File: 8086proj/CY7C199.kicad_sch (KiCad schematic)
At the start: 5 parts, among them U3 CY7C199, U4 CY7C199

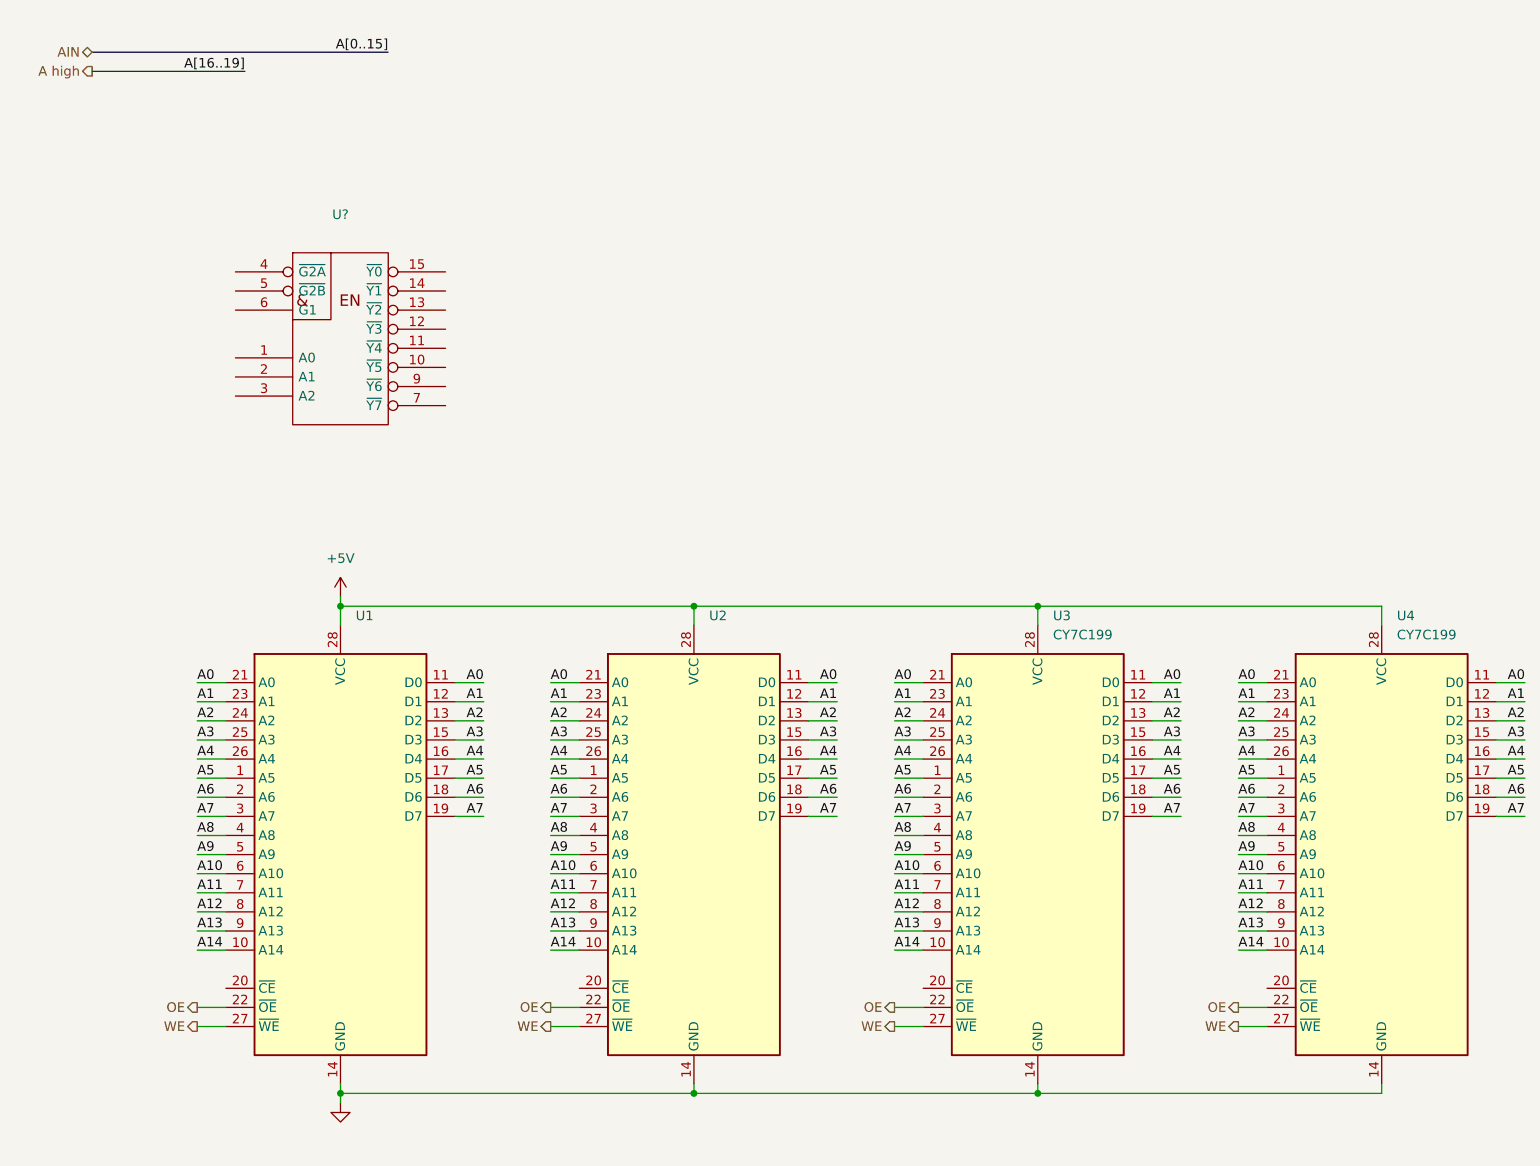
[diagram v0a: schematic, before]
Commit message: finished cy7c199
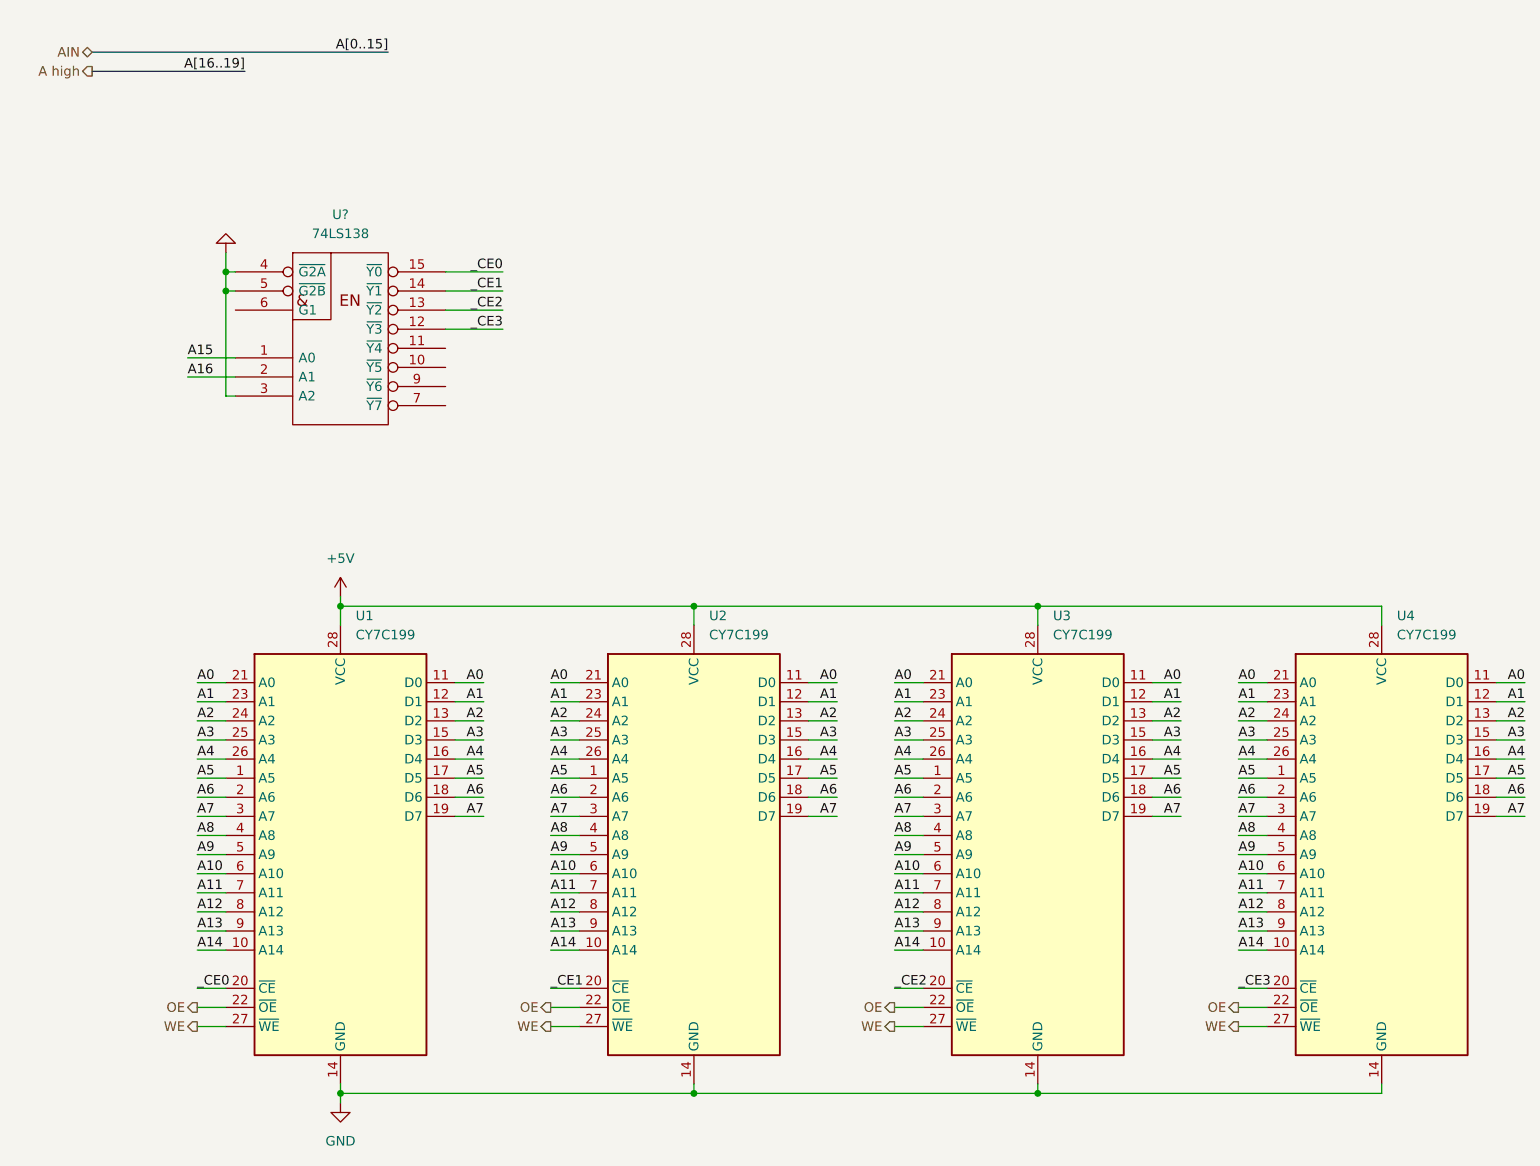
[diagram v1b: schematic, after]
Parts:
- U1, U2: value (none) -> CY7C199
- U?: value (none) -> 74LS138
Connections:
- net GND: now also U?.3 (A2), U?.4 (~{G2A}), U?.5 (~{G2B})
- net _CE3: now reaches U4.20 (~{CE})
- net _CE3: now also U?.12 (~{Y3})
- net _CE1: now reaches U2.20 (~{CE})
- net _CE1: now also U?.14 (~{Y1})
- net _CE0: now reaches U1.20 (~{CE})
- net _CE0: now also U?.15 (~{Y0})
- net A15: now reaches U?.1 (A0)
- net _CE2: now reaches U?.13 (~{Y2})
- net _CE2: now also U3.20 (~{CE})
- net A16: now reaches U?.2 (A1)
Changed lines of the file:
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@@
 (kicad_sch (version 20211123) (generator eeschema)
   (paper "A4")
+  (junction (at 52.07 49.53) (diameter 0) (color 0 0 0 0)
+  )
   (junction (at 67.31 156.21) (diameter 0) (color 0 0 0 0)
   )
   (junction (at 114.3 156.21) (diameter 0) (color 0 0 0 0)
   )
+  (junction (at 52.07 46.99) (diameter 0) (color 0 0 0 0)
+  )
   (junction (at 160.02 156.21) (diameter 0) (color 0 0 0 0)
   )
@@
     (stroke (width 0) (type default) (color 0 0 0 0))
   )
+  (wire (pts (xy 186.69 142.24) (xy 190.5 142.24))
+    (stroke (width 0) (type default) (color 0 0 0 0))
+  )
   (wire (pts (xy 220.98 109.22) (xy 224.79 109.22))
     (stroke (width 0) (type default) (color 0 0 0 0))
@@
     (stroke (width 0) (type default) (color 0 0 0 0))
   )
+  (wire (pts (xy 52.07 49.53) (xy 53.34 49.53))
+    (stroke (width 0) (type default) (color 0 0 0 0))
+  )
   (wire (pts (xy 140.97 104.14) (xy 144.78 104.14))
     (stroke (width 0) (type default) (color 0 0 0 0))
   )
+  (wire (pts (xy 46.99 60.96) (xy 53.34 60.96))
+    (stroke (width 0) (type default) (color 0 0 0 0))
+  )
   (wire (pts (xy 186.69 134.62) (xy 190.5 134.62))
     (stroke (width 0) (type default) (color 0 0 0 0))
@@
     (stroke (width 0) (type default) (color 0 0 0 0))
   )
+  (wire (pts (xy 52.07 46.99) (xy 53.34 46.99))
+    (stroke (width 0) (type default) (color 0 0 0 0))
+  )
   (wire (pts (xy 67.31 154.94) (xy 67.31 156.21))
     (stroke (width 0) (type default) (color 0 0 0 0))
@@
     (stroke (width 0) (type default) (color 0 0 0 0))
   )
+  (wire (pts (xy 95.25 142.24) (xy 99.06 142.24))
+    (stroke (width 0) (type default) (color 0 0 0 0))
+  )
   (wire (pts (xy 129.54 104.14) (xy 133.35 104.14))
     (stroke (width 0) (type default) (color 0 0 0 0))
@@
     (stroke (width 0) (type default) (color 0 0 0 0))
   )
+  (wire (pts (xy 52.07 44.45) (xy 52.07 46.99))
+    (stroke (width 0) (type default) (color 0 0 0 0))
+  )
   (wire (pts (xy 95.25 109.22) (xy 99.06 109.22))
     (stroke (width 0) (type default) (color 0 0 0 0))
@@
     (stroke (width 0) (type default) (color 0 0 0 0))
   )
+  (wire (pts (xy 46.99 58.42) (xy 53.34 58.42))
+    (stroke (width 0) (type default) (color 0 0 0 0))
+  )
   (wire (pts (xy 140.97 127) (xy 144.78 127))
     (stroke (width 0) (type default) (color 0 0 0 0))
@@
     (stroke (width 0) (type default) (color 0 0 0 0))
   )
+  (wire (pts (xy 81.28 46.99) (xy 88.9 46.99))
+    (stroke (width 0) (type default) (color 0 0 0 0))
+  )
   (wire (pts (xy 82.55 104.14) (xy 86.36 104.14))
     (stroke (width 0) (type default) (color 0 0 0 0))
@@
     (stroke (width 0) (type default) (color 0 0 0 0))
   )
+  (wire (pts (xy 48.26 142.24) (xy 52.07 142.24))
+    (stroke (width 0) (type default) (color 0 0 0 0))
+  )
   (wire (pts (xy 186.69 147.32) (xy 190.5 147.32))
     (stroke (width 0) (type default) (color 0 0 0 0))
@@
     (stroke (width 0) (type default) (color 0 0 0 0))
   )
+  (wire (pts (xy 52.07 46.99) (xy 52.07 49.53))
+    (stroke (width 0) (type default) (color 0 0 0 0))
+  )
   (wire (pts (xy 48.26 101.6) (xy 52.07 101.6))
     (stroke (width 0) (type default) (color 0 0 0 0))
   )
+  (wire (pts (xy 81.28 52.07) (xy 88.9 52.07))
+    (stroke (width 0) (type default) (color 0 0 0 0))
+  )
   (wire (pts (xy 114.3 91.44) (xy 114.3 93.98))
     (stroke (width 0) (type default) (color 0 0 0 0))
@@
     (stroke (width 0) (type default) (color 0 0 0 0))
   )
+  (wire (pts (xy 53.34 63.5) (xy 52.07 63.5))
+    (stroke (width 0) (type default) (color 0 0 0 0))
+  )
+  (wire (pts (xy 81.28 54.61) (xy 88.9 54.61))
+    (stroke (width 0) (type default) (color 0 0 0 0))
+  )
   (wire (pts (xy 95.25 101.6) (xy 99.06 101.6))
     (stroke (width 0) (type default) (color 0 0 0 0))
@@
     (stroke (width 0) (type default) (color 0 0 0 0))
   )
+  (wire (pts (xy 52.07 49.53) (xy 52.07 63.5))
+    (stroke (width 0) (type default) (color 0 0 0 0))
+  )
   (wire (pts (xy 48.26 104.14) (xy 52.07 104.14))
     (stroke (width 0) (type default) (color 0 0 0 0))
@@
     (stroke (width 0) (type default) (color 0 0 0 0))
   )
+  (wire (pts (xy 81.28 49.53) (xy 88.9 49.53))
+    (stroke (width 0) (type default) (color 0 0 0 0))
+  )
   (wire (pts (xy 48.26 127) (xy 52.07 127))
     (stroke (width 0) (type default) (color 0 0 0 0))
@@
     (stroke (width 0) (type default) (color 0 0 0 0))
   )
+  (wire (pts (xy 140.97 142.24) (xy 144.78 142.24))
+    (stroke (width 0) (type default) (color 0 0 0 0))
+  )
   (wire (pts (xy 186.69 104.14) (xy 190.5 104.14))
     (stroke (width 0) (type default) (color 0 0 0 0))
@@
     (effects (font (size 1.27 1.27)) (justify left bottom))
   )
+  (label "_CE3" (at 186.69 142.24 0)
+    (effects (font (size 1.27 1.27)) (justify left bottom))
+  )
   (label "A0" (at 86.36 101.6 180)
     (effects (font (size 1.27 1.27)) (justify right bottom))
@@
     (effects (font (size 1.27 1.27)) (justify left bottom))
   )
+  (label "_CE2" (at 140.97 142.24 0)
+    (effects (font (size 1.27 1.27)) (justify left bottom))
+  )
   (label "A7" (at 48.26 119.38 0)
     (effects (font (size 1.27 1.27)) (justify left bottom))
@@
     (effects (font (size 1.27 1.27)) (justify left bottom))
   )
+  (label "_CE0" (at 88.9 46.99 180)
+    (effects (font (size 1.27 1.27)) (justify right bottom))
+  )
   (label "A8" (at 140.97 121.92 0)
     (effects (font (size 1.27 1.27)) (justify left bottom))
@@
     (effects (font (size 1.27 1.27)) (justify left bottom))
   )
+  (label "A15" (at 46.99 58.42 0)
+    (effects (font (size 1.27 1.27)) (justify left bottom))
+  )
   (label "A11" (at 95.25 129.54 0)
     (effects (font (size 1.27 1.27)) (justify left bottom))
   )
+  (label "_CE3" (at 88.9 54.61 180)
+    (effects (font (size 1.27 1.27)) (justify right bottom))
+  )
+  (label "_CE1" (at 88.9 49.53 180)
+    (effects (font (size 1.27 1.27)) (justify right bottom))
+  )
+  (label "_CE1" (at 95.25 142.24 0)
+    (effects (font (size 1.27 1.27)) (justify left bottom))
+  )
   (label "A2" (at 224.79 106.68 180)
     (effects (font (size 1.27 1.27)) (justify right bottom))
@@
     (effects (font (size 1.27 1.27)) (justify right bottom))
   )
+  (label "_CE2" (at 88.9 52.07 180)
+    (effects (font (size 1.27 1.27)) (justify right bottom))
+  )
   (label "A10" (at 140.97 127 0)
     (effects (font (size 1.27 1.27)) (justify left bottom))
@@
     (effects (font (size 1.27 1.27)) (justify right bottom))
   )
+  (label "A16" (at 46.99 60.96 0)
+    (effects (font (size 1.27 1.27)) (justify left bottom))
+  )
   (label "A6" (at 95.25 116.84 0)
     (effects (font (size 1.27 1.27)) (justify left bottom))
@@
   )
   (label "A8" (at 186.69 121.92 0)
+    (effects (font (size 1.27 1.27)) (justify left bottom))
+  )
+  (label "_CE0" (at 48.26 142.24 0)
     (effects (font (size 1.27 1.27)) (justify left bottom))
   )
@@
       (effects (font (size 1.27 1.27)) hide)
     )
-    (property "Value" "" (id 1) (at 67.31 162.56 0))
+    (property "Value" "GND" (id 1) (at 67.31 162.56 0))
     (property "Footprint" "" (id 2) (at 67.31 157.48 0)
       (effects (font (size 1.27 1.27)) hide)
@@
       (effects (font (size 1.27 1.27)) (justify left))
     )
-    (property "Value" "" (id 1) (at 116.3194 95.25 0)
+    (property "Value" "CY7C199" (id 1) (at 116.3194 95.25 0)
       (effects (font (size 1.27 1.27)) (justify left))
     )
@@
       (effects (font (size 1.27 1.27)) (justify left))
     )
-    (property "Value" "" (id 1) (at 69.3294 95.25 0)
+    (property "Value" "CY7C199" (id 1) (at 69.3294 95.25 0)
       (effects (font (size 1.27 1.27)) (justify left))
     )
@@
     (pin "9")
   )
+  (symbol (lib_id "power:GND") (at 52.07 44.45 180) (unit 1)
+    (in_bom yes) (on_board yes) (fields_autoplaced)
+    (property "Reference" "#PWR?" (id 0) (at 52.07 38.1 0)
+      (effects (font (size 1.27 1.27)) hide)
+    )
+    (property "Value" "" (id 1) (at 52.07 39.37 0))
+    (property "Footprint" "" (id 2) (at 52.07 44.45 0)
+      (effects (font (size 1.27 1.27)) hide)
+    )
+    (property "Datasheet" "" (id 3) (at 52.07 44.45 0)
+      (effects (font (size 1.27 1.27)) hide)
+    )
+    (pin "1")
+  )
   (symbol (lib_id "74xx_IEEE:74LS138") (at 67.31 52.07 0) (unit 1)
     (in_bom yes) (on_board yes) (fields_autoplaced)
     (property "Reference" "U?" (id 0) (at 67.31 39.37 0))
-    (property "Value" "" (id 1) (at 67.31 41.91 0))
+    (property "Value" "74LS138" (id 1) (at 67.31 41.91 0))
     (property "Footprint" "" (id 2) (at 67.31 52.07 0)
       (effects (font (size 1.27 1.27)) hide)

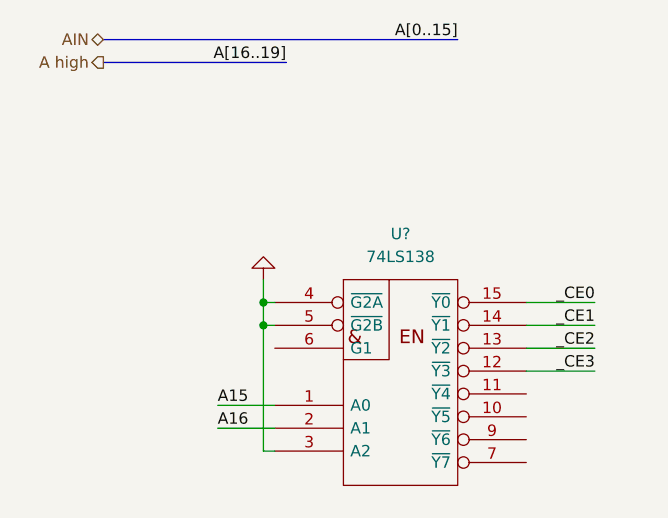
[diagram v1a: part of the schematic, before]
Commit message: 28F010 fix
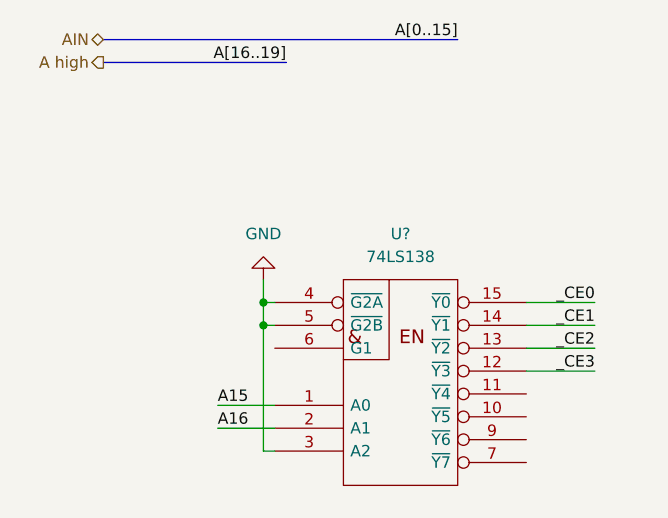
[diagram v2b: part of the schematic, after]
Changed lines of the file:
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@@
       (effects (font (size 1.27 1.27)) hide)
     )
-    (property "Value" "" (id 1) (at 52.07 39.37 0))
+    (property "Value" "GND" (id 1) (at 52.07 39.37 0))
     (property "Footprint" "" (id 2) (at 52.07 44.45 0)
       (effects (font (size 1.27 1.27)) hide)

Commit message: 8259
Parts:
- removed U?: 74LS138, symbol 74xx_IEEE:74LS138
- added C0, C1, C2, C3: (no value), symbol Device:C
- added C?: .1uF, symbol Device:C
- added U0: (no value), symbol Logic_Programmable:PAL16L8
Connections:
- net _CE2 is gone; now on net _CE1: U3.20 (~{CE})
- net _CE3 is gone; now on net _CE1: U4.20 (~{CE})
- net A0: no longer U1.11 (D0), U2.11 (D0), U3.11 (D0), U4.11 (D0)
- net A1: no longer U1.12 (D1), U2.12 (D1), U3.12 (D1), U4.12 (D1)
- net A16: now also U0.1 (I1)
- net A2: no longer U1.13 (D2), U2.13 (D2), U3.13 (D2), U4.13 (D2)
- net A3: no longer U1.15 (D3), U2.15 (D3), U3.15 (D3), U4.15 (D3)
- net A4: no longer U1.16 (D4), U2.16 (D4), U3.16 (D4), U4.16 (D4)
- net A5: no longer U1.17 (D5), U2.17 (D5), U3.17 (D5), U4.17 (D5)
- net A6: no longer U1.18 (D6), U2.18 (D6), U3.18 (D6), U4.18 (D6)
- net A7: no longer U1.19 (D7), U2.19 (D7), U3.19 (D7), U4.19 (D7)
- net GND: now also C0.1, C1.1, C2.1, C3.1, C?.1, U0.10 (GND)
- net _CE0: now also U2.20 (~{CE}), U0.19 (IO1)
- net _CE1: now also U0.18 (IO2); no longer U2.20 (~{CE})
- net +5V renamed VIN
- net VIN: now also C0.2, C1.2, C2.2, C3.2, C?.2, U0.20 (VCC)
- new net D0: U1.11 (D0), U3.11 (D0)
- new net D1: U1.12 (D1), U3.12 (D1)
- new net D10: U2.13 (D2), U4.13 (D2)
- new net D11: U2.15 (D3), U4.15 (D3)
- new net D12: U2.16 (D4), U4.16 (D4)
- new net D13: U2.17 (D5), U4.17 (D5)
- new net D14: U2.18 (D6), U4.18 (D6)
- new net D15: U2.19 (D7), U4.19 (D7)
- new net D2: U1.13 (D2), U3.13 (D2)
- new net D3: U1.15 (D3), U3.15 (D3)
- new net D4: U1.16 (D4), U3.16 (D4)
- new net D5: U1.17 (D5), U3.17 (D5)
- new net D6: U1.18 (D6), U3.18 (D6)
- new net D7: U1.19 (D7), U3.19 (D7)
- new net D8: U2.11 (D0), U4.11 (D0)
- new net D9: U2.12 (D1), U4.12 (D1)
- no-connect marks 0 -> 15

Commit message: fixes
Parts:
- C0, C1, C2, C3: value (none) -> .1uF
- U0: value (none) -> PAL16L8
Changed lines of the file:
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@@
       (effects (font (size 1.27 1.27)) (justify left))
     )
-    (property "Value" "" (id 1) (at 111.7599 83.82 0)
+    (property "Value" ".1uF" (id 1) (at 111.7599 83.82 0)
       (effects (font (size 1.27 1.27)) (justify left))
     )
@@
       (effects (font (size 1.27 1.27)) (justify left))
     )
-    (property "Value" "" (id 1) (at 203.1999 83.82 0)
+    (property "Value" ".1uF" (id 1) (at 203.1999 83.82 0)
       (effects (font (size 1.27 1.27)) (justify left))
     )
@@
       (effects (font (size 1.27 1.27)) hide)
     )
-    (property "Value" "" (id 1) (at 45.72 72.39 0))
+    (property "Value" "GND" (id 1) (at 45.72 72.39 0))
     (property "Footprint" "" (id 2) (at 45.72 67.31 0)
       (effects (font (size 1.27 1.27)) hide)
@@
       (effects (font (size 1.27 1.27)) (justify left))
     )
-    (property "Value" "" (id 1) (at 47.7394 35.56 0)
+    (property "Value" "PAL16L8" (id 1) (at 47.7394 35.56 0)
       (effects (font (size 1.27 1.27)) (justify left))
     )
@@
       (effects (font (size 1.27 1.27)) (justify left))
     )
-    (property "Value" "" (id 1) (at 64.7699 83.82 0)
+    (property "Value" ".1uF" (id 1) (at 64.7699 83.82 0)
       (effects (font (size 1.27 1.27)) (justify left))
     )
@@
       (effects (font (size 1.27 1.27)) (justify left))
     )
-    (property "Value" "" (id 1) (at 157.4799 83.82 0)
-      (effects (font (size 1.27 1.27)) (justify left))
-    )
+    (property "Value" ".1uF" (id 1) (at 157.4799 83.82 0)
+      (effects (font (size 1.27 1.27)) (justify left))
+    )

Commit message: 74244
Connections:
- net M/_IO: now reaches U0.2 (I2)
- no-connect marks 15 -> 14
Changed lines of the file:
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@@
   (no_connect (at 33.02 49.53))
   (no_connect (at 33.02 46.99))
-  (no_connect (at 33.02 41.91))
   (no_connect (at 33.02 44.45))
   (no_connect (at 58.42 44.45))
@@
     (effects (font (size 1.27 1.27)) (justify right))
   )
+  (hierarchical_label "M{slash}_IO" (shape output) (at 33.02 41.91 180)
+    (effects (font (size 1.27 1.27)) (justify right))
+  )

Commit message: fixes
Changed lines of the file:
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@@
     (effects (font (size 1.27 1.27)) (justify left bottom))
+  )
+  (label "VIN" (at 43.18 20.32 180)
+    (effects (font (size 1.27 1.27)) (justify right bottom))
   )
   (label "A10" (at 95.25 127 0)
